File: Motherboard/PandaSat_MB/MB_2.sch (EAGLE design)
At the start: 125 parts, among them J1 503182-1852, J10 1445055-5, J2 10118194-0001LF, J3 DCJ0303, J4 1445055-5, J5 1445055-5, J6 1445055-5, J7 BK-18650, J8 1445055-5, J9 1445055-5, Q10 IRLML5103, Q11 IRLML5103, Q13 IRLML2803, Q14 IRLML2803, Q15 IRLML2803, Q16 IRLML5103, Q17 2N5088, Q2 32.768, U1 MAX706R, U11 DRV8848, U12 DRV8848, U13 DRV8848, U2 LTC4121-4.2, U3 LSM9DS1, U4 PE014006, U5 MAX4372TEUK+T, U6 RFM23BP, U7 TPS54226PWPRPWP14_2P31X2P46-L, U8 ATSAMD51, U9 OKL-T3-W12, X1 BU-SMA-V

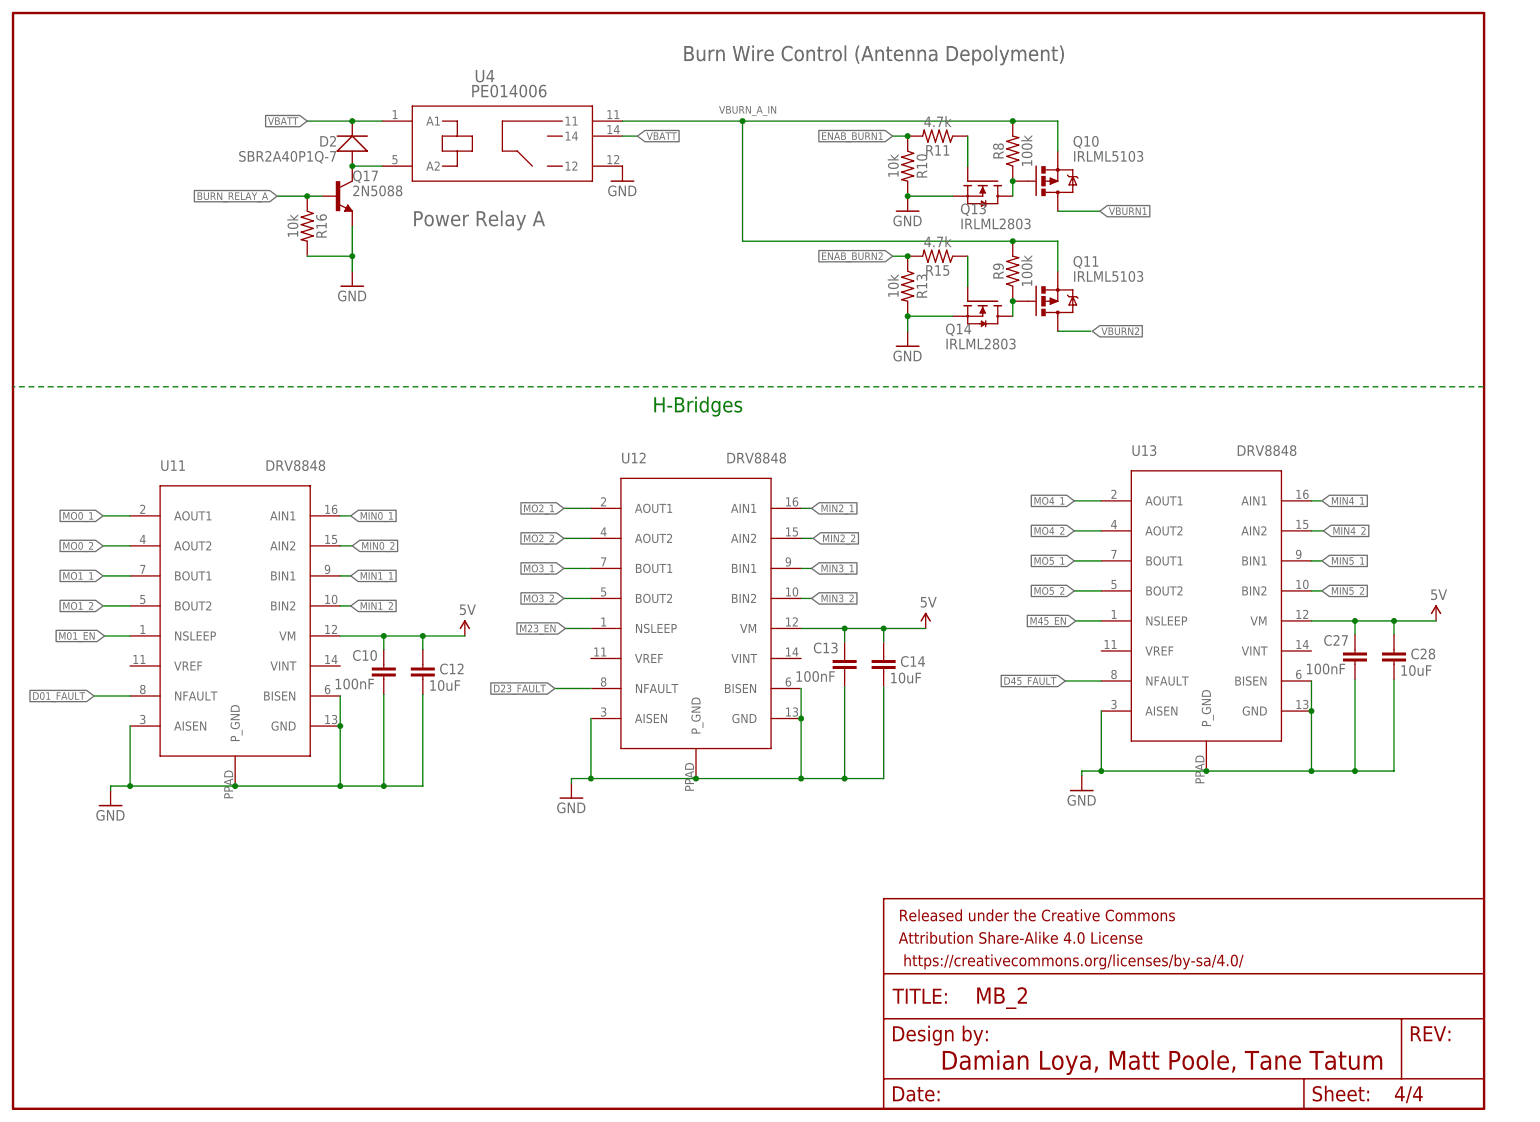
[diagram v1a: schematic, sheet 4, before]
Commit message: Fixed H-Bridge circuits
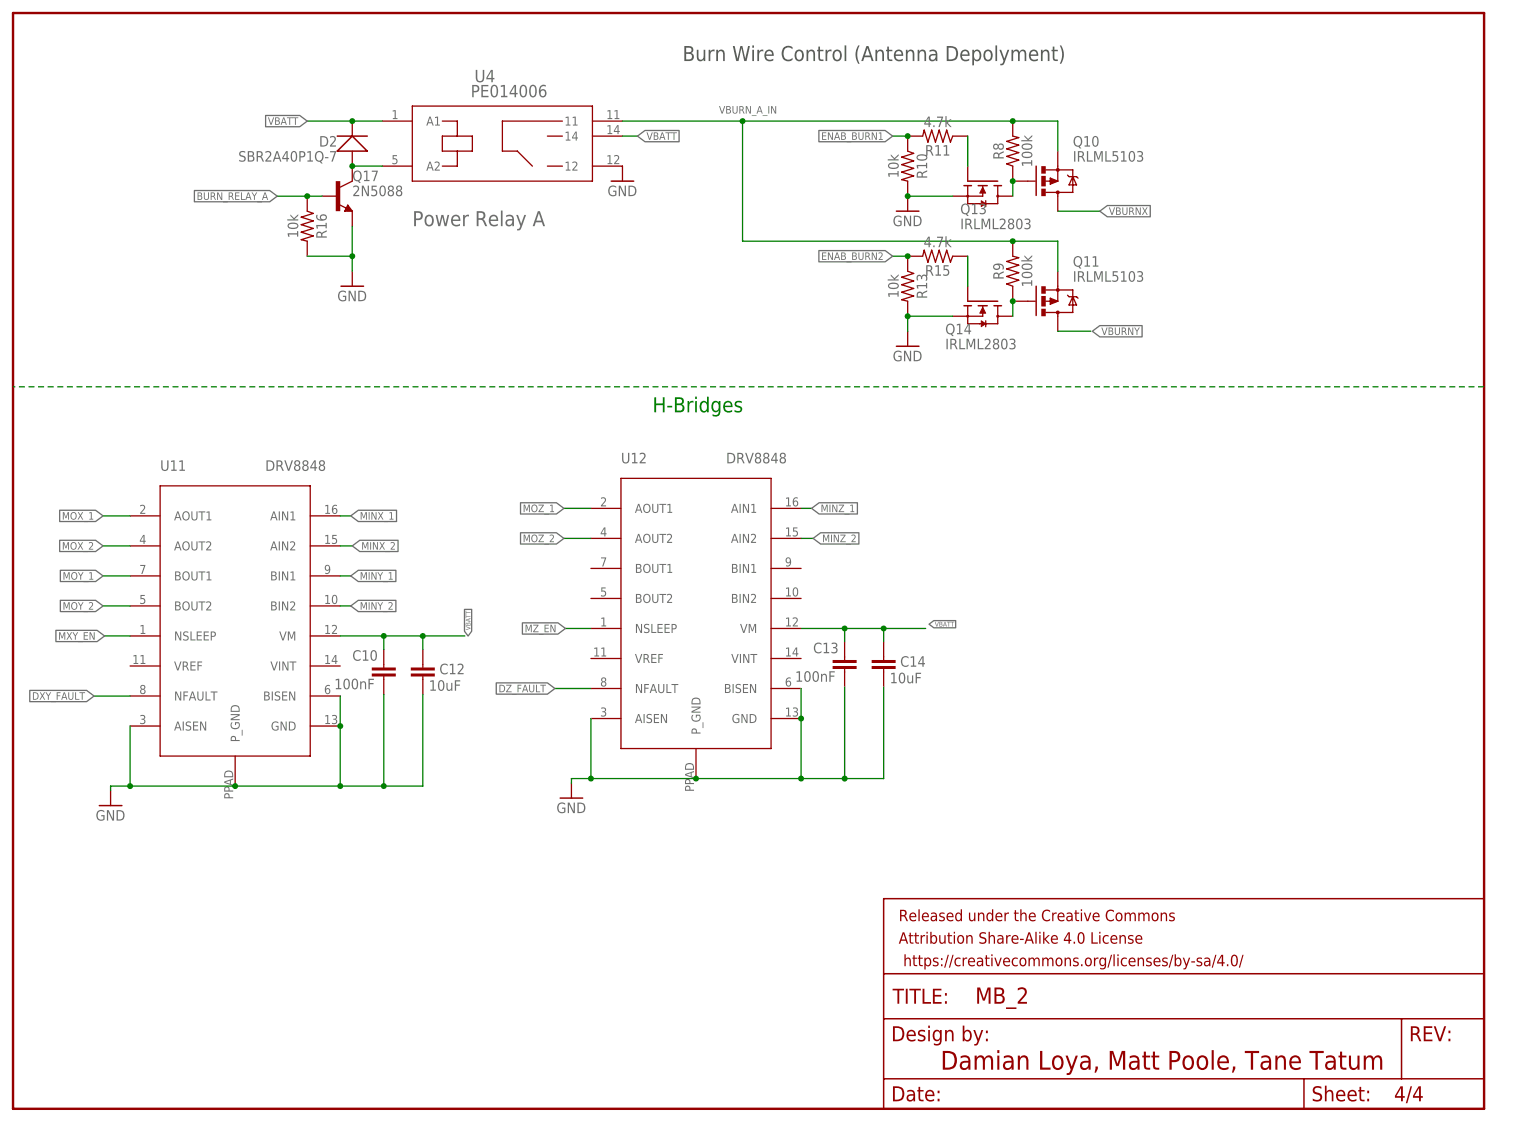
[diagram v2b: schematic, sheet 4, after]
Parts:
- removed C27: 100nF, SparkFun-Capacitors:10UF-0603-6.3V-20%
- removed C28: 10uF, SparkFun-Capacitors:10UF-0603-6.3V-20%
- removed U13: DRV8848, pandasat:DRV8848
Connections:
- net D01_FAULT renamed DXY_FAULT
- net D23_FAULT renamed DZ_FAULT
- net M01_EN renamed MXY_EN
- net M23_EN renamed MZ_EN
- net MIN0_1 renamed MINX_1
- net MIN0_2 renamed MINX_2
- net MIN1_1 renamed MINY_1
- net MIN1_2 renamed MINY_2
- net MIN2_1 renamed MINZ_1
- net MIN2_2 renamed MINZ_2
- net MO0_1 renamed MOX_1
- net VBURN1 renamed VBURNX
- removed net D45_FAULT: U13.NFAULT
- removed net M45_EN: U13.NSLEEP
- removed net MIN3_1: U12.BIN1
- removed net MIN3_2: U12.BIN2
- removed net MIN4_1: U13.AIN1
- removed net MIN4_2: U13.AIN2
- removed net MIN5_1: U13.BIN1
- removed net MIN5_2: U13.BIN2
- removed net MO0_2: J5.4, U11.AOUT2
- removed net MO1_1: J4.3, U11.BOUT1
- removed net MO1_2: J4.4, U11.BOUT2
- removed net MO2_1: J6.3, U12.AOUT1
- removed net MO2_2: J6.4, U12.AOUT2
- removed net MO3_1: J8.3, U12.BOUT1
- removed net MO3_2: J8.4, U12.BOUT2
- removed net MO4_1: J9.3, U13.AOUT1
- removed net MO4_2: J9.4, U13.AOUT2
- removed net MO5_1: J10.3, U13.BOUT1
- removed net MO5_2: J10.4, U13.BOUT2
- removed net N$27: J8.5
- removed net VBURN2: J4.5, Q11.D
- new net MOX_2: J4.4, U11.AOUT2
- new net MOX_MID: J4.3, J5.4
- new net MOY_1: J6.3, U11.BOUT1
- new net MOY_2: J8.4, U11.BOUT2
- new net MOY_MID: J6.4, J8.3
- new net MOZ_1: J9.3, U12.AOUT1
- new net MOZ_2: J10.4, U12.AOUT2
- new net MOZ_MID: J10.3, J9.4
- new net VBURNY: J4.5, J6.5, J8.5, Q11.D
- net 5V: no longer C10.1, C12.1, C13.1, C14.1, C27.1, C28.1, U11.VM, U12.VM, U13.VM
- net GND: no longer C27.2, C28.2, U13.AISEN, U13.BISEN, U13.GND, U13.P_GND
- net VBATT: now also C10.1, C12.1, C13.1, C14.1, U11.VM, U12.VM

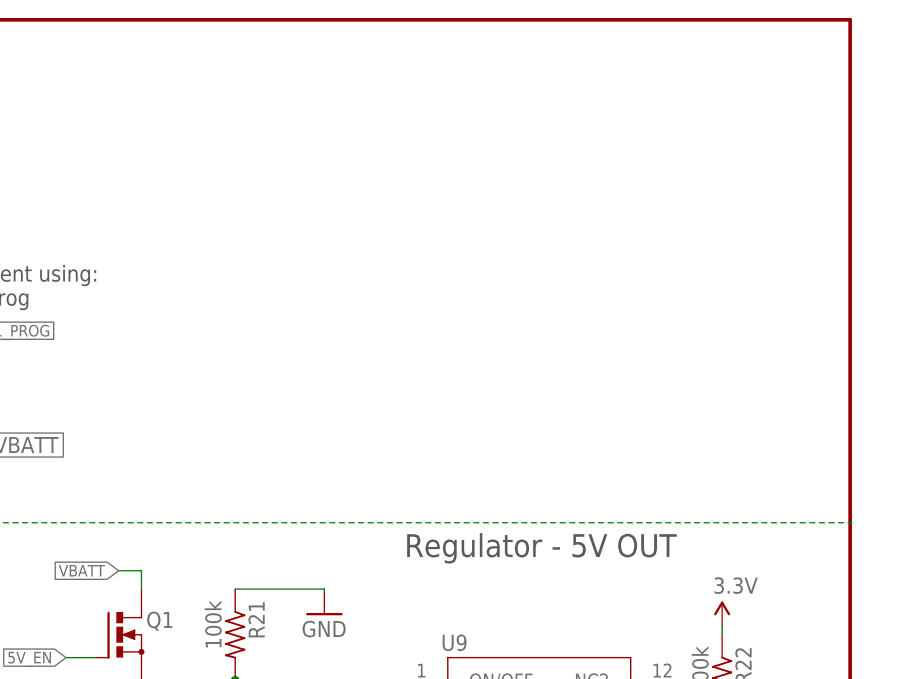
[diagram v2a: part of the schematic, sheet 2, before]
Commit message: Added LEDS, Added decoupling Caps for MCU, Labeled Analog Pins
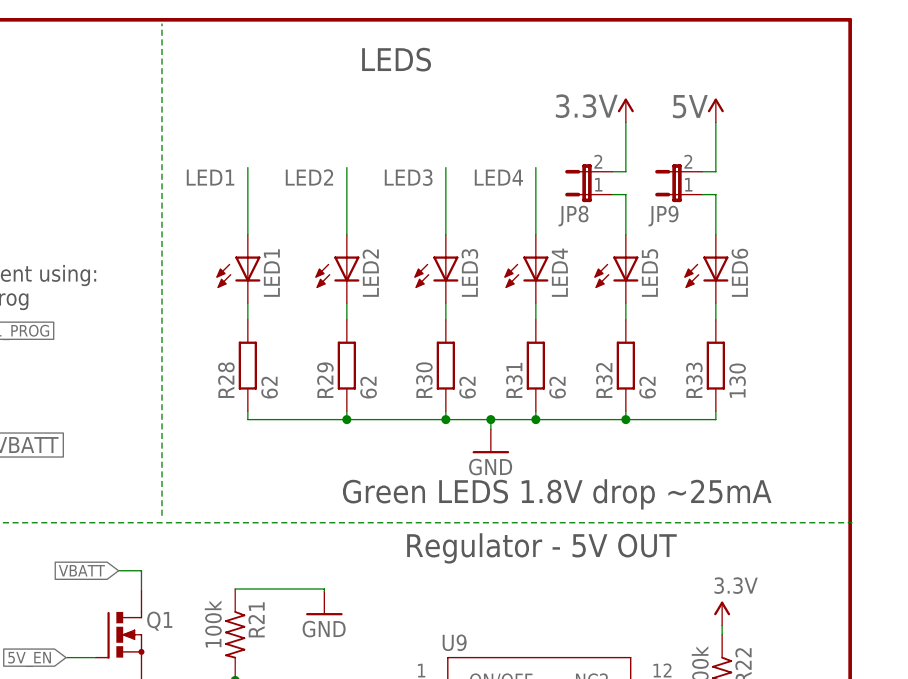
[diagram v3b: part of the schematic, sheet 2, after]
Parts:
- added C27, C34, C35: 1uF, resistor:C-EUC0603
- added C28: 10uF, resistor:C-EUC0603
- added JP7, JP8, JP9: (no value), jumper:JP1E
- added LED1, LED2, LED3, LED4, LED5, LED6: (no value), led:LEDCHIPLED-0603-TTW
- added R28, R29, R30, R31, R32: 62, resistor:R-EU_R0603
- added R33: 130, resistor:R-EU_R0603
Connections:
- new net A0: U8.PA02
- new net A1: U8.PA05
- new net A2: U8.PB08
- new net A3: U8.PB09
- new net A4: U8.PA04
- new net A5: U8.PA06
- new net AIN: U8.PA07
- new net AREF: C27.2, JP7.1, U8.PA03
- new net LED1: LED1.A, U8.PB03
- new net LED2: LED2.A, U8.PB04
- new net LED3: LED3.A, U8.PA14
- new net LED4: LED4.A, U8.PA15
- new net N$27: LED1.C, R28.2
- new net N$45: LED2.C, R29.2
- new net N$47: LED3.C, R30.2
- new net N$48: LED4.C, R31.2
- new net N$49: LED5.C, R32.2
- new net N$50: LED6.C, R33.2
- new net N$53: JP8.1, LED5.A
- new net N$55: JP9.1, LED6.A
- net 3.3V: now also C28.2, C34.2, C35.2, JP7.2, JP8.2
- net 5V: now also JP9.2
- net GND: now also C27.1, C28.1, C34.1, C35.1, R28.1, R29.1, R30.1, R31.1, R32.1, R33.1
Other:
- note added: "Green LEDS 1.8V drop ~25mA"
- note added: "LEDS"

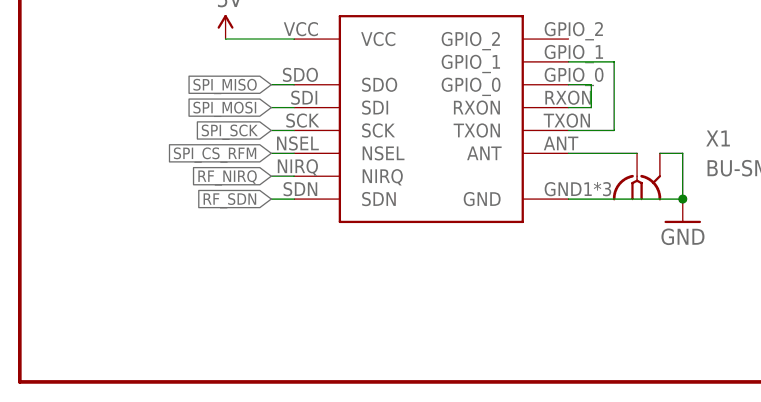
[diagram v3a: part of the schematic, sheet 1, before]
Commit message: Added Todos, testing Slack notification
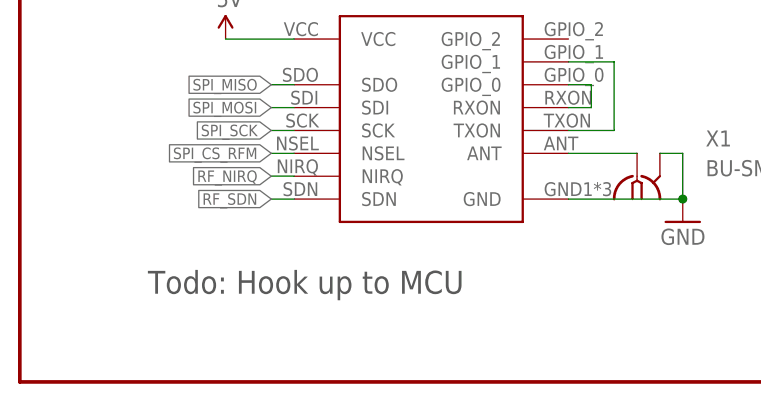
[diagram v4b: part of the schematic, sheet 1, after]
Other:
- note added: "Todo: Hook up to MCU"
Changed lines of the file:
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@@
 <text x="131.94" y="179.8" size="2.54" layer="97">SAM51 MCU</text>
 <text x="152.94" y="6.62" size="3.175" layer="94">Damian Loya, Matt Poole, Tane Tatum</text>
+<text x="14.24" y="12.34" size="2.54" layer="97" align="top-left">Todo: Hook up to MCU</text>
 </plain>
 <instances>

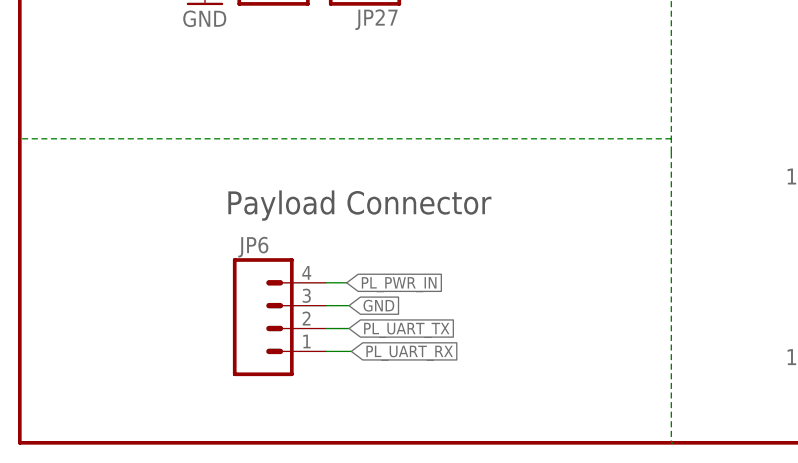
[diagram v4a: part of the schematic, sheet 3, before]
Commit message: Replaced 4-pin payload connector with 6-pin connector
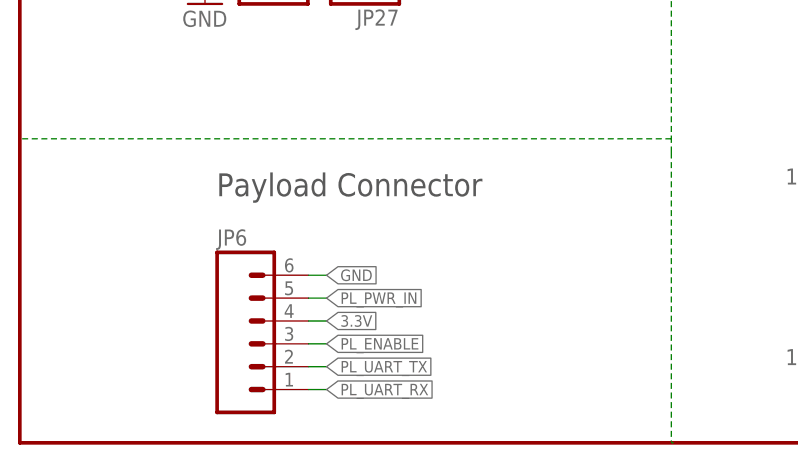
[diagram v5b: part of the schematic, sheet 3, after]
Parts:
- JP6: device SparkFun-Connectors:M04JST-PTH-VERT -> SparkFun-Connectors:M06POLAR
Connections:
- net ENAB_PAYLOAD renamed PL_PWR_ENAB
- new net PL_ENABLE: JP6.3
- net 3.3V: now also JP6.4
- net GND: now also JP6.6; no longer JP6.3
- net PL_PWR_IN: now also JP6.5; no longer JP6.4
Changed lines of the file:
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@@
 <?xml version="1.0" encoding="utf-8"?>
 <!DOCTYPE eagle SYSTEM "eagle.dtd">
-<eagle version="9.2.2">
+<eagle version="9.3.0">
 <drawing>
 <settings>
@@
 <part name="J10" library="con-amp" library_urn="urn:adsk.eagle:library:127" deviceset="1445055-5" device=""/>
 <part name="FRAME4" library="SparkFun-Aesthetics" deviceset="FRAME-LETTER" device=""/>
-<part name="JP6" library="SparkFun-Connectors" deviceset="M04" device="JST-PTH-VERT"/>
 <part name="U8" library="pandasat" deviceset="ATSAMD51" device=""/>
 <part name="C29" library="resistor" library_urn="urn:adsk.eagle:library:348" deviceset="C-EU" device="C0805" package3d_urn="urn:adsk.eagle:package:26137/1" value="1uF"/>
@@
 <part name="JP8" library="jumper" library_urn="urn:adsk.eagle:library:252" deviceset="JP1E" device="" package3d_urn="urn:adsk.eagle:package:15455/1"/>
 <part name="JP9" library="jumper" library_urn="urn:adsk.eagle:library:252" deviceset="JP1E" device="" package3d_urn="urn:adsk.eagle:package:15455/1"/>
+<part name="JP6" library="SparkFun-Connectors" deviceset="M06" device="POLAR"/>
 </parts>
 <sheets>
@@
 </segment>
 </net>
-<net name="ENAB_PAYLOAD" class="0">
+<net name="PL_PWR_ENAB" class="0">
 <segment>
 <wire x1="180.34" y1="53.34" x2="177.8" y2="53.34" width="0.1524" layer="91"/>
@@
 Connection</text>
 <text x="96.012" y="53.34" size="2.54" layer="97" align="top-left">Solar Panel Connectors</text>
-<text x="22.86" y="27.94" size="2.54" layer="97" align="top-left">Payload Connector</text>
+<text x="21.86" y="29.94" size="2.54" layer="97" align="top-left">Payload Connector</text>
 <text x="109.982" y="130.81" size="1.778" layer="97">Batterys in 2s2p config</text>
 </plain>
@@
 <attribute name="VALUE" x="131.064" y="10.16" size="1.778" layer="96" rot="R180"/>
 </instance>
-<instance part="JP6" gate="G$1" x="28.956" y="12.7" smashed="yes">
-<attribute name="VALUE" x="23.876" y="5.08" size="1.778" layer="96"/>
-<attribute name="NAME" x="24.384" y="21.082" size="1.778" layer="95"/>
-</instance>
 <instance part="D4" gate="G$1" x="205.426" y="158.31" smashed="yes" rot="R270">
 <attribute name="NAME" x="207.966" y="158.31" size="1.778" layer="95" rot="R270"/>
 <attribute name="VALUE" x="200.346" y="161.866" size="1.778" layer="96" rot="R270"/>
+</instance>
+<instance part="JP6" gate="G$1" x="27" y="11" smashed="yes">
+<attribute name="VALUE" x="21.92" y="0.84" size="1.778" layer="96"/>
+<attribute name="NAME" x="21.92" y="21.922" size="1.778" layer="95"/>
 </instance>
 </instances>
@@
 </segment>
 <segment>
-<pinref part="JP6" gate="G$1" pin="3"/>
-<wire x1="34.036" y1="15.24" x2="36.576" y2="15.24" width="0.1524" layer="91"/>
-<label x="36.576" y="15.24" size="1.27" layer="95" xref="yes"/>
+<pinref part="JP6" gate="G$1" pin="6"/>
+<wire x1="32.08" y1="18.62" x2="34.08" y2="18.62" width="0.1524" layer="91"/>
+<label x="34.08" y="18.62" size="1.27" layer="95" xref="yes"/>
 </segment>
 </net>
@@
 <wire x1="58.42" y1="110.998" x2="60.96" y2="110.998" width="0.1524" layer="91"/>
 <wire x1="60.96" y1="110.998" x2="60.96" y2="113.538" width="0.1524" layer="91"/>
+</segment>
+<segment>
+<pinref part="JP6" gate="G$1" pin="4"/>
+<wire x1="32.08" y1="13.54" x2="34.08" y2="13.54" width="0.1524" layer="91"/>
+<label x="34.08" y="13.54" size="1.27" layer="95" xref="yes"/>
 </segment>
 </net>
@@
 <segment>
 <pinref part="JP6" gate="G$1" pin="1"/>
-<wire x1="34.036" y1="10.16" x2="36.83" y2="10.16" width="0.1524" layer="91"/>
-<label x="36.83" y="10.16" size="1.27" layer="95" xref="yes"/>
+<wire x1="32.08" y1="5.92" x2="34.08" y2="5.92" width="0.1524" layer="91"/>
+<label x="34.08" y="5.92" size="1.27" layer="95" xref="yes"/>
 </segment>
 </net>
@@
 <segment>
 <pinref part="JP6" gate="G$1" pin="2"/>
-<wire x1="34.036" y1="12.7" x2="36.576" y2="12.7" width="0.1524" layer="91"/>
-<label x="36.576" y="12.7" size="1.27" layer="95" xref="yes"/>
+<wire x1="32.08" y1="8.46" x2="34.08" y2="8.46" width="0.1524" layer="91"/>
+<label x="34.08" y="8.46" size="1.27" layer="95" xref="yes"/>
 </segment>
 </net>
 <net name="PL_PWR_IN" class="0">
 <segment>
-<pinref part="JP6" gate="G$1" pin="4"/>
-<wire x1="34.036" y1="17.78" x2="36.322" y2="17.78" width="0.1524" layer="91"/>
-<label x="36.322" y="17.78" size="1.27" layer="95" xref="yes"/>
+<pinref part="JP6" gate="G$1" pin="5"/>
+<wire x1="32.08" y1="16.08" x2="34.08" y2="16.08" width="0.1524" layer="91"/>
+<label x="34.08" y="16.08" size="1.27" layer="95" xref="yes"/>
 </segment>
 </net>
@@
 </segment>
 </net>
+<net name="PL_ENABLE" class="0">
+<segment>
+<pinref part="JP6" gate="G$1" pin="3"/>
+<wire x1="32.08" y1="11" x2="34.08" y2="11" width="0.1524" layer="91"/>
+<label x="34.08" y="11" size="1.27" layer="95" xref="yes"/>
+</segment>
+</net>

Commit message: Routed communication lines and analog signals, changed 5V regulator circuit
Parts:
- removed L1: 3.3uH, BrownSpaceEngineering:IND1812
- added R34: 10K, resistor:R-US_R0603
- added R36: 10k, resistor:R-US_R0603
- C7: value 10uF -> 22uF
- C9: value 10uF -> 47uF
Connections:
- removed net A0: U8.PA02
- removed net A1: U8.PA05
- removed net MISO: U8.PB22
- removed net MOSI: U8.PB23
- removed net N$22: L1.P$2, U9.VOUT1
- removed net RX_D0: U8.PB17
- removed net SPI_CS_MRAM: U10.SSEL
- removed net TX_D1: U8.PB16
- removed net USB_D+: J2.D+
- removed net USB_D-: J2.D-
- new net QSPI_CS: R36.2, U10.SSEL, U8.PB11
- new net QSPI_DATA[0]: U10.MOSI, U8.PA08
- new net QSPI_DATA[1]: U10.MISO, U8.PA09
- new net QSPI_DATA[2]: U10.#WP/IO2, U8.PA10
- new net QSPI_DATA[3]: U10.#HOLD/IO3, U8.PA11
- new net QSPI_SCK: U10.SCK, U8.PB10
- new net USB_N: J2.D-, U8.PA24
- new net USB_P: J2.D+, U8.PA25
- net 3.3V: now also R34.2, R36.1
- net 5V: now also U9.VOUT1; no longer L1.P$1
- net I_BATT: now also U8.PA05
- net L1_PROG: now also U8.PA02
- net MINX_1: now also U8.PA18
- net MINX_2: now also U8.PA19
- net MINY_1: now also U8.PA20
- net MINY_2: now also U8.PA21
- net MINZ_1: now also U8.PA22
- net MINZ_2: now also U8.PA23
- net PL_UART_RX: now also U8.PB17
- net PL_UART_TX: now also U8.PB16
- net SPI_MISO: now also U8.PB22; no longer U10.MISO
- net SPI_MOSI: now also U8.PB23; no longer U10.MOSI
- net SPI_SCK: now also U8.PA17; no longer U10.SCK
- net SWCLK: now also R34.1, U8.PA30
- net SWDIO: now also U8.PA31
- net VBURNX: now also J4.5
- net VBURNY: no longer J4.5
